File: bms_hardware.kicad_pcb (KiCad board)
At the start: 2 copper layers, 176 parts, among them J2 Conn_01x07_Female, J3 Vcc In, J4 CH_TS, J5 Conn_01x05_Male, Q1 2N7002, Q10 FDD86580-F085, Q11 BC848, Q12 BC848, Q13 IRF9310PbF, Q2 2N7002, Q3 2N7002, Q4 2N7002, Q5 2N7002, Q6 2N7002, Q7 DMP4051LK3, Q8 DMP4051LK3, Q9 FDD86580-F085, SW1 Reset, SW2 Select CE, SW3 SW_Push, U1 INA226, U2 BQ76PL536A, U3 BQ24618RGET, U4 TPS54331D, U5 FERD2045SB-TR, U6 STM32F407VGTx, Y1 8MHz

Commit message: Adds final pcb
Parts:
- added +(BATT): MountingHole_Pad, MountingHole:MountingHole_3mm_Pad_TopBottom, F.Cu at (231.6, 119.3)
- added +(LOAD): MountingHole_Pad, MountingHole:MountingHole_3mm_Pad_TopBottom, F.Cu at (193.6, 146.5)
- added -(LOAD): MountingHole_Pad, MountingHole:MountingHole_3mm_Pad_TopBottom, F.Cu at (173.6, 146.3)
- added C59: 330nF, Capacitor_SMD:C_0805_2012Metric_Pad1.18x1.45mm_HandSolder, F.Cu at (126.3, 140.2)
- added C60: 100nF, Capacitor_SMD:C_0805_2012Metric_Pad1.18x1.45mm_HandSolder, F.Cu at (105.7, 132.9)
- added C61: 4.7uF, Capacitor_SMD:C_0805_2012Metric_Pad1.18x1.45mm_HandSolder, F.Cu at (97.3, 136.5)
- added C62: 100pF, Capacitor_SMD:C_0805_2012Metric_Pad1.18x1.45mm_HandSolder, F.Cu at (99.7, 133.2)
- added C63: 100pF, Capacitor_SMD:C_0805_2012Metric_Pad1.18x1.45mm_HandSolder, F.Cu at (99.7, 139.6)
- added G***: LOGO, Symbol:unr_logo, F.Cu at (164.5, 86.0)
- added G***: LOGO, Symbol:fceia_logo, F.Cu at (178.1, 86.1)
- added H1: MountingHole, MountingHole:MountingHole_3.2mm_M3_Pad_Via, F.Cu at (231.1, 86.2)
- added H2: MountingHole, MountingHole:MountingHole_3.2mm_M3_Pad_Via, F.Cu at (230.6, 147.5)
- added H3: MountingHole, MountingHole:MountingHole_3.2mm_M3_Pad_Via, F.Cu at (90.6, 86.3)
- added H4: MountingHole, MountingHole:MountingHole_3.2mm_M3_Pad_Via, F.Cu at (90.3, 148.1)
- added J1: Conn_01x04_Male, Connector_PinHeader_2.54mm:PinHeader_1x04_P2.54mm_Vertical, F.Cu at (132.9, 146.7)
- added J6: DB9_Male, Connector_Dsub:DSUB-9_Male_Horizontal_P2.77x2.84mm_EdgePinOffset4.94mm_Housed_MountingHolesOffset7.48mm, F.Cu at (108.0, 144.8)
- added R5: 100, Resistor_SMD:R_0805_2012Metric_Pad1.20x1.40mm_HandSolder, F.Cu at (105.2, 140.5)
- added R6: 60, Resistor_SMD:R_0805_2012Metric_Pad1.20x1.40mm_HandSolder, F.Cu at (101.5, 135.3)
- added R7: 60, Resistor_SMD:R_0805_2012Metric_Pad1.20x1.40mm_HandSolder, F.Cu at (101.5, 137.5)
- added U7: PDM1-S12-S3-S, Converter_DCDC:CONV_PDM1-S12-S3-S, F.Cu at (125.5, 131.9)
- added U8: SN65HVD233, Package_SO:SOIC-8_3.9x4.9mm_P1.27mm, F.Cu at (108.8, 136.7)
- added U9: INA226, Package_SO:VSSOP-10_3x3mm_P0.5mm, F.Cu at (206.2, 135.1)
- C43: moved to B.Cu
- NT1: footprint NetTie:NetTie-3_SMD_Pad0.5mm -> NetTie:NetTie-2_SMD_Pad2.0mm; moved to B.Cu
- SW3: footprint Button_Switch_SMD:SW_SPST_TL3305A -> Button_Switch_THT:SW_PUSH_6mm_H4.3mm
- U1: value INA226 -> ADuM1201AR; footprint Package_SO:VSSOP-10_3x3mm_P0.5mm -> Package_SO:SOIC-8_3.9x4.9mm_P1.27mm
- U2: value BQ76PL536A -> BQ76PL536APAPR; footprint Package_QFP:HTQFP-64-1EP_10x10mm_P0.5mm_EP8x8mm -> Package_QFP:HTQFP-64-1EP_10x10mm_P0.5mm_EP8x8mm_Mask4.4x4.4mm_ThermalVias
- U3: footprint Package_DFN_QFN:VQFN-24-1EP_4x4mm_P0.5mm_EP2.45x2.45mm -> Package_DFN_QFN:VQFN-24-1EP_4x4mm_P0.5mm_EP2.45x2.45mm_ThermalVias
- U5: footprint Package_TO_SOT_SMD:TO-263-3_TabPin2 -> Package_TO_SOT_SMD:TO-252-2
- moved R65 165.8 mm to (193.3, 132.1), turned to 180 degrees
- moved R64 163.8 mm to (193.3, 134.2), turned to 180 degrees
- moved Q12 163.1 mm to (193.3, 137.1)
- moved Q13 162.4 mm to (207.7, 142.9)
- moved R63 159.6 mm to (185.5, 137.1), turned to 180 degrees
- moved Q11 158.1 mm to (185.5, 134.1), turned to 180 degrees
- moved U5 153.4 mm to (216.5, 141.7)
- moved D20 138.6 mm to (189.3, 135.2), turned to 270 degrees
- moved C58 97.1 mm to (144.2, 133.4), turned to 270 degrees
- moved J4 92.3 mm to (193.1, 91.0), turned to 180 degrees
- moved SW2 85.7 mm to (184.5, 104.2)
- moved SW1 81.2 mm to (180.0, 95.8), turned to 0 degrees
- moved NT1 80.8 mm to (197.8, 120.7), turned to 180 degrees
- moved U1 66.7 mm to (120.4, 136.9), turned to 180 degrees
- moved C38 50.1 mm to (135.6, 94.0), turned to 270 degrees
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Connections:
- net /bat_charger/GNDA renamed GND1
- net PA13 renamed SWDIO
- net PA14 renamed SWCLK
- C32 pad 1: +24V -> +BATT
- C34 pad 1: +24V -> +BATT
- C35 pad 1: +24V -> +BATT
- R1 pad 1: +24V -> +BATT
- R45 pad 1: /bat_charger/PG -> /mcu_stm32f407/BQ24_PG
- R46 pad 1: /bat_charger/STAT2 -> /mcu_stm32f407/BQ24_STAT2
- R47 pad 1: /bat_charger/STAT1 -> /mcu_stm32f407/BQ24_STAT1
- R52 pad 1: +24V -> +BATT
- R55 pad 1: +24V -> +BATT
- SW2 pad 2: /bat_charger/uCE -> /mcu_stm32f407/BQ24_CE
- U1 pad 1: GND -> VBAT
- U1 pad 2: GND -> /mcu_stm32f407/CAN_1RX
- U1 pad 3: /current_sensor_ina226/ALERT_INA226 -> /mcu_stm32f407/CAN_1TX
- U1 pad 4: /current_sensor_ina226/SDA -> GND
- U1 pad 5: /current_sensor_ina226/SCL -> GND2
- U1 pad 6: VBAT -> ISO_CAN_TX
- U1 pad 7: GND -> ISO_CAN_RX
- U1 pad 8: +24V -> Net-(U1-Pad8)
- U2 pad 47: GND -> Net-(U2-Pad47)
- U2 pad 48: GND -> Net-(U2-Pad47)
- U3 pad 13: +24V -> +BATT
- U3 pad 5: /bat_charger/STAT1 -> /mcu_stm32f407/BQ24_STAT1
- U3 pad 8: /bat_charger/PG -> /mcu_stm32f407/BQ24_PG
- U3 pad 9: /bat_charger/STAT2 -> /mcu_stm32f407/BQ24_STAT2
- U5 pad 2: GND -> /bat_switch/D
- U5 pad 3: /bat_switch/D -> GND
- U6 pad 1: Net-(U6-Pad1) -> /bat_switch/G
- U6 pad 15: Net-(U6-Pad15) -> /mcu_stm32f407/BQ24_PG
- U6 pad 16: Net-(U6-Pad16) -> /mcu_stm32f407/BQ24_STAT2
- U6 pad 17: Net-(U6-Pad17) -> /mcu_stm32f407/BQ24_STAT1
- U6 pad 18: Net-(U6-Pad18) -> /mcu_stm32f407/BQ24_CE
- U6 pad 80: Net-(U6-Pad80) -> UART_TX
- U6 pad 83: Net-(U6-Pad83) -> UART_RX
- U6 pad 91: /bat_switch/G -> Net-(U6-Pad91)
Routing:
- net GND: track 96.7 -> 353.6 mm, vias 0 -> 10
- net GND1: track 2.03 -> 246.5 mm, vias 1 -> 7
- net VBAT: track 120.5 -> 290.7 mm, vias 1 -> 4
- net /current_sensor_ina226/SCL: track 2.28 -> 68.2 mm, vias 0 -> 2
- net /current_sensor_ina226/SDA: track 5.29 -> 68.0 mm, vias 0 -> 2
- net /mcu_stm32f407/BQ24_PG: track 0.00 -> 58.0 mm, vias 0 -> 4
- net /mcu_stm32f407/BQ24_STAT2: track 0.00 -> 54.5 mm, vias 0 -> 4
- net /mcu_stm32f407/BQ24_STAT1: track 0.00 -> 53.6 mm, vias 0 -> 4
- net +BATT: track 0.00 -> 50.4 mm
- net Net-(R36-Pad2): track 0.00 -> 47.1 mm, vias 0 -> 1
- net /mcu_stm32f407/BQ24_CE: track 0.00 -> 45.4 mm
- net /bat_switch/G: track 0.00 -> 41.3 mm, vias 0 -> 2
- net /bat_charger/VREF: track 20.4 -> 60.9 mm, vias 0 -> 5
- net Net-(J4-Pad2): track 6.56 -> 46.6 mm
- net /can_hw/CANH: track 0.00 -> 26.1 mm
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- added copper zone on B.Cu, net +BATT
- added copper zone on F.Cu, net +BATT
- added copper zone on B.Cu, net /LOAD_OUTPUT+
- added copper zone on F.Cu, net /LOAD_OUTPUT+
- added copper zone on B.Cu, net /bat_switch/D
- added copper zone on F.Cu, net /bat_switch/D
- added copper zone on B.Cu, net GND
- added copper zone on F.Cu, net GND
- added copper zone on B.Cu, net GND1
- added copper zone on B.Cu, net GND2
- added copper zone on F.Cu, net GND2
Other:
- board outline added: 150.6 x 71.7 mm
- board text added: "BMS_UNR - Proyecto Final CECCARELLI, Federico MOYA, Martin SANTOS, Lucio"

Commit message: Mirrors in x axis J3
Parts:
- removed G***: LOGO, Symbol:unr_logo
- removed G***: LOGO, Symbol:fceia_logo
- renumbered +(BATT) to +(BATT)1, +(LOAD) to +(LOAD)1, -(LOAD) to -(LOAD)1
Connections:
- J3 pad 1: GND1 -> Net-(D13-Pad1)
- J3 pad 2: Net-(D13-Pad1) -> GND1
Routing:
- net GND1: track 246.5 -> 190.2 mm
- net Net-(D13-Pad1): track 34.9 -> 29.7 mm

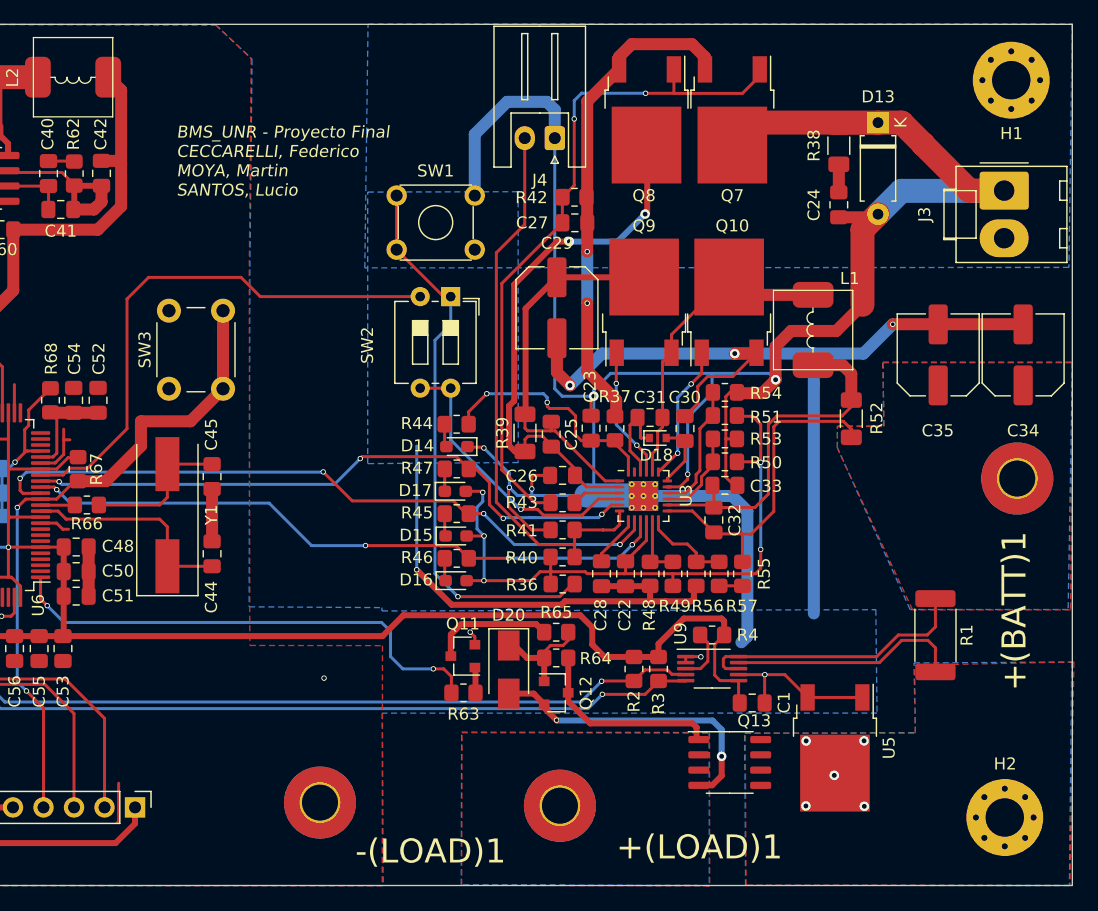
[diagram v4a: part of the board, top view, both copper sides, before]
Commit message: Reorder battery connection pins
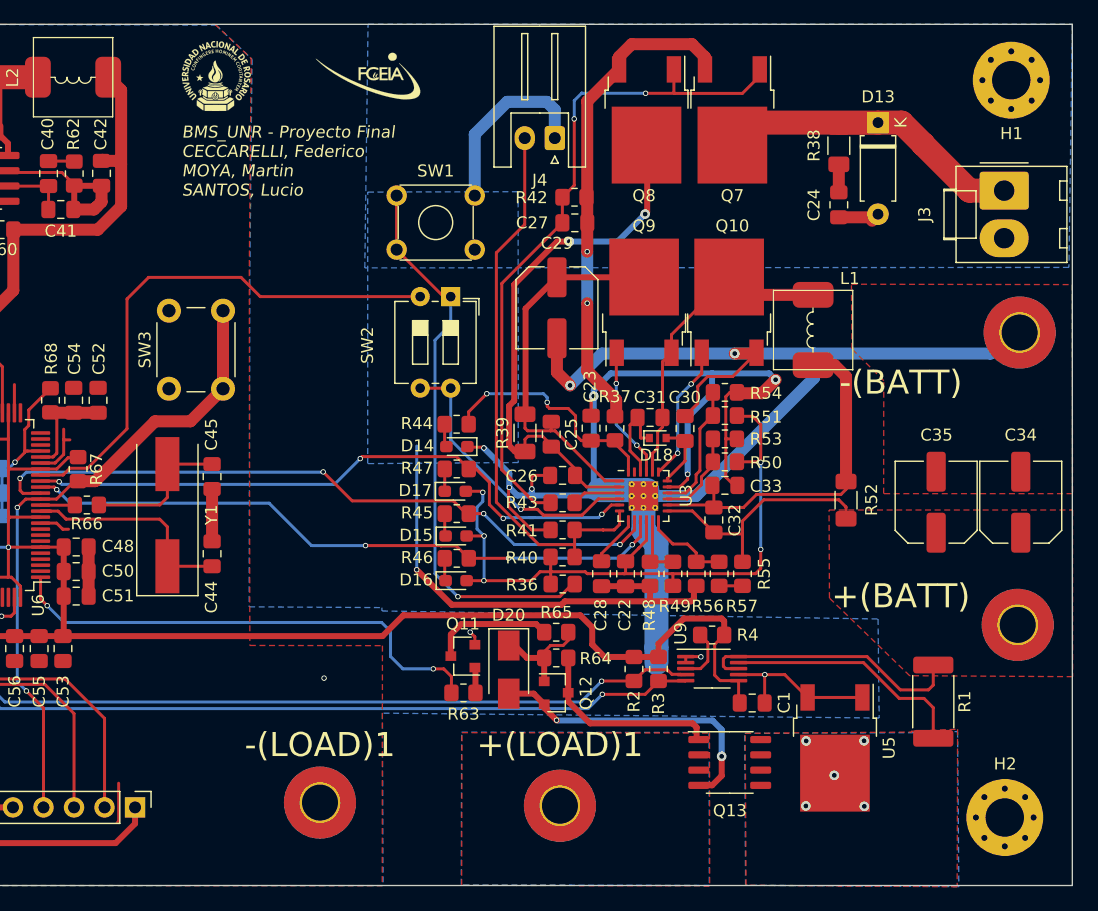
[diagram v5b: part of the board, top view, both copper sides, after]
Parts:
- added -(BATT): MountingHole_Pad, MountingHole:MountingHole_3mm_Pad_TopBottom, F.Cu at (231.8, 107.2)
- added G***: LOGO, Symbol:fceia_logo, F.Cu at (177.5, 86.0)
- added G***: LOGO, Symbol:unr_logo, F.Cu at (165.0, 85.8)
- moved C34 12.3 mm to (231.9, 121.3)
- moved C35 12.3 mm to (224.9, 121.3)
- moved +(BATT) 12.2 mm to (231.7, 131.5)
- moved R52 6.79 mm to (217.4, 121.1)
- moved R1 5.53 mm to (224.6, 137.9)
- moved NT1 1.16 mm to (198.8, 120.3)
- renumbered +(BATT)1 to +(BATT)
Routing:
- net GND1: track 190.2 -> 136.9 mm
- net GND: track 353.6 -> 345.7 mm, vias 10 -> 9
- net +BATT: track 50.4 -> 43.7 mm
- net NRST: track 54.8 -> 53.6 mm
- net /bat_switch/D: track 19.4 -> 20.3 mm
- removed copper zone on B.Cu, net +BATT

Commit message: Minor fix
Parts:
- NT1: footprint NetTie:NetTie-2_SMD_Pad2.0mm -> NetTie:NetTie-2_SMD_Pad0.5mm
- moved D17 0.13 mm to (185.0, 120.4)
- moved D15 0.06 mm to (185.0, 124.1)
- moved D16 0.06 mm to (185.0, 127.8)

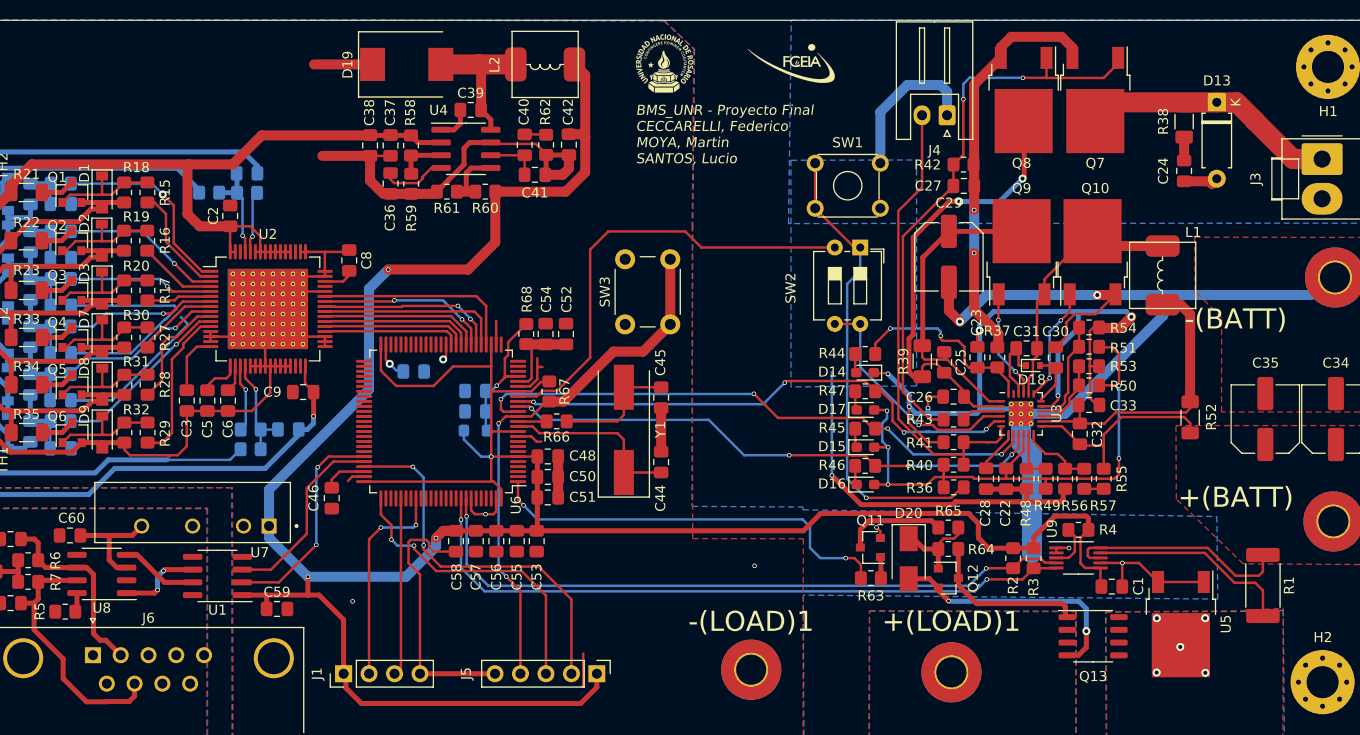
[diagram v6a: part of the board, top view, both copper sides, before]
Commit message: Minor changes to 3v3 buck converter
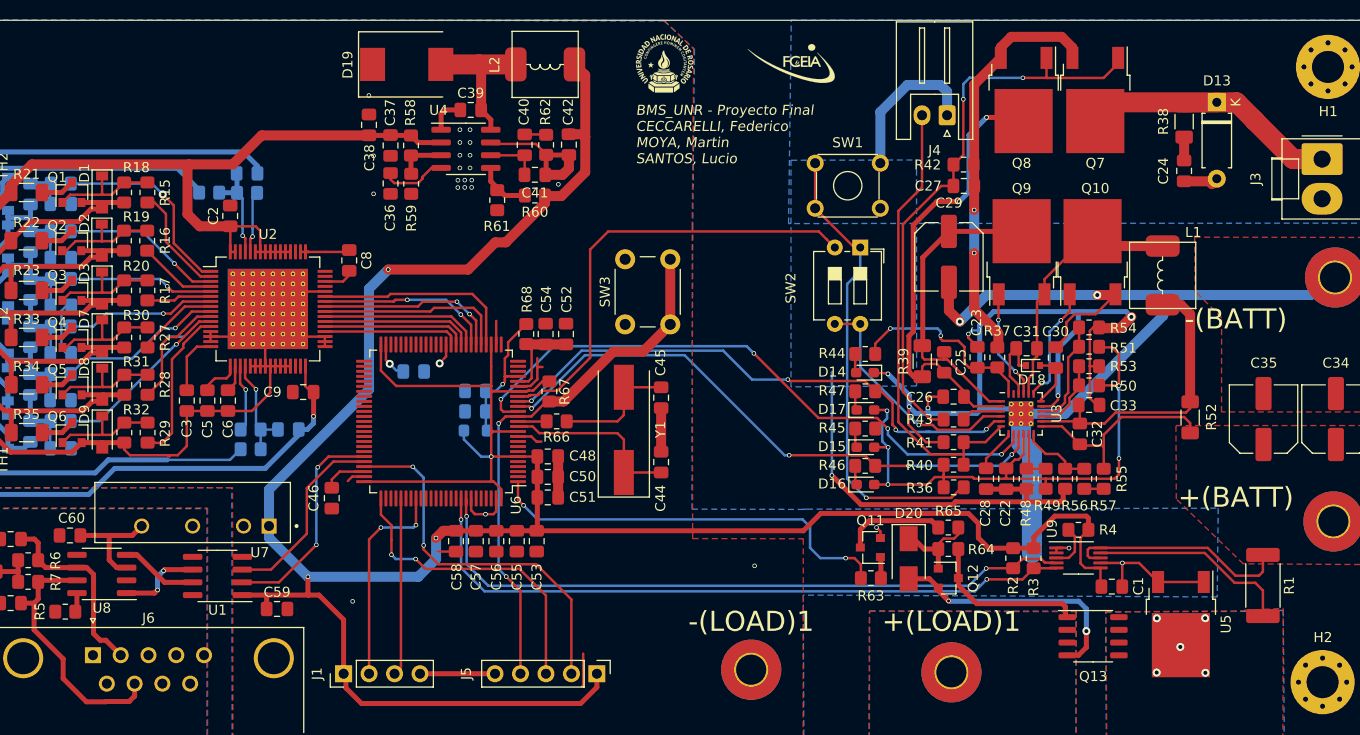
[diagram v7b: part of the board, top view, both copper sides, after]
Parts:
- moved R61 5.09 mm to (148.3, 99.4), turned to 270 degrees
- moved R60 4.96 mm to (152.0, 99.0)
- moved C38 2.05 mm to (135.5, 91.9), turned to 90 degrees
- moved C35 0.18 mm to (224.7, 121.3)
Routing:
- net GND: track 345.7 -> 254.4 mm, vias 9 -> 27
- net /mcu_stm32f407/BQ24_STAT2: track 54.5 -> 58.9 mm
- net /mcu_stm32f407/BQ24_PG: track 58.0 -> 62.3 mm
- net /mcu_stm32f407/BQ24_STAT1: track 53.6 -> 56.2 mm
- net VBAT: track 290.7 -> 288.1 mm
- net GND1: track 136.9 -> 138.2 mm
- net VSENSE: track 6.32 -> 5.32 mm
- net /bat_charger/ACP: track 45.9 -> 46.9 mm
- net VDDA: track 14.9 -> 15.7 mm
- net Net-(C27-Pad2): track 57.3 -> 58.0 mm
- net SWCLK: track 30.3 -> 31.0 mm
